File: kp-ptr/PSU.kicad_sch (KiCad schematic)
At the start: 23 parts, among them J2 Conn_01x02, J3 Conn_01x02, U8 AZ1117CH-5.0TRG1, U9 LDFM33PVR

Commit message: Update from v0.1 to v1.0
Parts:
- C35, C36: value 10u -> 10uF 6V3; footprint Capacitor_SMD:C_0402_1005Metric -> Capacitor_SMD:C_0603_1608Metric
- C37: value 1uF -> 100n
- C38: value 1uF -> 100n 50V
- F1: footprint Fuse:Fuse_0805_2012Metric -> Fuse:Fuse_1210_3225Metric
- R19: value 100k -> 100k 1%
- R20: value 10k -> 10k 1%
- R23: value 20k -> 22k
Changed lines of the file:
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@@
     (in_bom yes) (on_board yes)
     (property "Reference" "R23" (id 0) (at 239.395 83.185 90))
-    (property "Value" "20k" (id 1) (at 244.475 83.185 90))
+    (property "Value" "22k" (id 1) (at 244.475 83.185 90))
     (property "Footprint" "Resistor_SMD:R_0402_1005Metric" (id 2) (at 240.157 81.915 90)
       (effects (font (size 1.27 1.27)) hide)
@@
       (effects (font (size 1.27 1.27)) (justify left))
     )
-    (property "Footprint" "Fuse:Fuse_0805_2012Metric" (id 2) (at 181.61 102.235 0)
+    (property "Footprint" "Fuse:Fuse_1210_3225Metric" (id 2) (at 181.61 102.235 0)
       (effects (font (size 1.27 1.27)) (justify left) hide)
     )
@@
   (symbol (lib_id "Device:C") (at 179.07 35.56 0) (mirror y) (unit 1)
     (in_bom yes) (on_board yes) (fields_autoplaced)
-    (property "Reference" "C36" (id 0) (at 175.26 34.2899 0)
-      (effects (font (size 1.27 1.27)) (justify left))
-    )
-    (property "Value" "10u" (id 1) (at 175.26 36.8299 0)
-      (effects (font (size 1.27 1.27)) (justify left))
-    )
-    (property "Footprint" "Capacitor_SMD:C_0402_1005Metric" (id 2) (at 178.1048 39.37 0)
+    (property "Reference" "C36" (id 0) (at 182.88 34.2899 0)
+      (effects (font (size 1.27 1.27)) (justify right))
+    )
+    (property "Value" "10uF 6V3" (id 1) (at 182.88 36.8299 0)
+      (effects (font (size 1.27 1.27)) (justify right))
+    )
+    (property "Footprint" "Capacitor_SMD:C_0603_1608Metric" (id 2) (at 178.1048 39.37 0)
       (effects (font (size 1.27 1.27)) hide)
     )
@@
     (in_bom yes) (on_board yes)
     (property "Reference" "R20" (id 0) (at 29.845 102.87 90))
-    (property "Value" "10k" (id 1) (at 34.925 102.87 90))
+    (property "Value" "10k 1%" (id 1) (at 34.925 102.87 90))
     (property "Footprint" "Resistor_SMD:R_0402_1005Metric" (id 2) (at 30.607 101.6 90)
       (effects (font (size 1.27 1.27)) hide)
@@
   (symbol (lib_id "Device:C") (at 111.76 38.1 0) (mirror y) (unit 1)
     (in_bom yes) (on_board yes) (fields_autoplaced)
-    (property "Reference" "C37" (id 0) (at 107.95 36.8299 0)
-      (effects (font (size 1.27 1.27)) (justify left))
-    )
-    (property "Value" "1uF" (id 1) (at 107.95 39.3699 0)
-      (effects (font (size 1.27 1.27)) (justify left))
+    (property "Reference" "C37" (id 0) (at 115.57 36.8299 0)
+      (effects (font (size 1.27 1.27)) (justify right))
+    )
+    (property "Value" "100n" (id 1) (at 115.57 39.3699 0)
+      (effects (font (size 1.27 1.27)) (justify right))
     )
     (property "Footprint" "Capacitor_SMD:C_0402_1005Metric" (id 2) (at 110.7948 41.91 0)
@@
   (symbol (lib_id "Device:C") (at 182.88 104.775 0) (mirror y) (unit 1)
     (in_bom yes) (on_board yes) (fields_autoplaced)
-    (property "Reference" "C35" (id 0) (at 179.07 103.5049 0)
-      (effects (font (size 1.27 1.27)) (justify left))
-    )
-    (property "Value" "10u" (id 1) (at 179.07 106.0449 0)
-      (effects (font (size 1.27 1.27)) (justify left))
-    )
-    (property "Footprint" "Capacitor_SMD:C_0402_1005Metric" (id 2) (at 181.9148 108.585 0)
+    (property "Reference" "C35" (id 0) (at 186.69 103.5049 0)
+      (effects (font (size 1.27 1.27)) (justify right))
+    )
+    (property "Value" "10uF 6V3" (id 1) (at 186.69 106.0449 0)
+      (effects (font (size 1.27 1.27)) (justify right))
+    )
+    (property "Footprint" "Capacitor_SMD:C_0603_1608Metric" (id 2) (at 181.9148 108.585 0)
       (effects (font (size 1.27 1.27)) hide)
     )
@@
   (symbol (lib_id "Device:C") (at 102.87 104.775 0) (mirror y) (unit 1)
     (in_bom yes) (on_board yes) (fields_autoplaced)
-    (property "Reference" "C38" (id 0) (at 99.06 103.5049 0)
-      (effects (font (size 1.27 1.27)) (justify left))
-    )
-    (property "Value" "1uF" (id 1) (at 99.06 106.0449 0)
-      (effects (font (size 1.27 1.27)) (justify left))
+    (property "Reference" "C38" (id 0) (at 106.68 103.5049 0)
+      (effects (font (size 1.27 1.27)) (justify right))
+    )
+    (property "Value" "100n 50V" (id 1) (at 106.68 106.0449 0)
+      (effects (font (size 1.27 1.27)) (justify right))
     )
     (property "Footprint" "Capacitor_SMD:C_0402_1005Metric" (id 2) (at 101.9048 108.585 0)
@@
     (in_bom yes) (on_board yes)
     (property "Reference" "R19" (id 0) (at 29.845 95.25 90))
-    (property "Value" "100k" (id 1) (at 34.925 95.25 90))
+    (property "Value" "100k 1%" (id 1) (at 34.925 92.71 90))
     (property "Footprint" "Resistor_SMD:R_0402_1005Metric" (id 2) (at 30.607 93.98 90)
       (effects (font (size 1.27 1.27)) hide)

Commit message: Work in progress
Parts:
- F1: footprint Fuse:Fuse_1210_3225Metric -> Fuse:Fuse_1206_3216Metric
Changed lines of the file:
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@@
       (effects (font (size 1.27 1.27)) (justify left))
     )
-    (property "Footprint" "Fuse:Fuse_1210_3225Metric" (id 2) (at 181.61 102.235 0)
+    (property "Footprint" "Fuse:Fuse_1206_3216Metric" (id 2) (at 181.61 102.235 0)
       (effects (font (size 1.27 1.27)) (justify left) hide)
     )

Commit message: Igniters rework v2
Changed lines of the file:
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@@
   (symbol (lib_id "power:+3.3V") (at 252.095 70.485 0) (unit 1)
     (in_bom yes) (on_board yes)
-    (property "Reference" "#PWR099" (id 0) (at 252.095 74.295 0)
+    (property "Reference" "#PWR0101" (id 0) (at 252.095 74.295 0)
       (effects (font (size 1.27 1.27)) hide)
     )
@@
   (symbol (lib_id "power:Earth") (at 182.88 108.585 0) (mirror y) (unit 1)
     (in_bom yes) (on_board yes) (fields_autoplaced)
-    (property "Reference" "#PWR087" (id 0) (at 182.88 114.935 0)
+    (property "Reference" "#PWR0113" (id 0) (at 182.88 114.935 0)
       (effects (font (size 1.27 1.27)) hide)
     )
@@
   (symbol (lib_id "power:VBUS") (at 56.515 33.655 0) (unit 1)
     (in_bom yes) (on_board yes) (fields_autoplaced)
-    (property "Reference" "#PWR082" (id 0) (at 56.515 37.465 0)
+    (property "Reference" "#PWR090" (id 0) (at 56.515 37.465 0)
       (effects (font (size 1.27 1.27)) hide)
     )
@@
   (symbol (lib_id "power:VCC") (at 57.15 44.45 0) (unit 1)
     (in_bom yes) (on_board yes)
-    (property "Reference" "#PWR083" (id 0) (at 57.15 48.26 0)
+    (property "Reference" "#PWR096" (id 0) (at 57.15 48.26 0)
       (effects (font (size 1.27 1.27)) hide)
     )
@@
   (symbol (lib_id "power:Earth") (at 262.255 85.725 0) (unit 1)
     (in_bom yes) (on_board yes) (fields_autoplaced)
-    (property "Reference" "#PWR0102" (id 0) (at 262.255 92.075 0)
+    (property "Reference" "#PWR0105" (id 0) (at 262.255 92.075 0)
       (effects (font (size 1.27 1.27)) hide)
     )
@@
   (symbol (lib_id "power:+3.3V") (at 179.07 31.75 0) (mirror y) (unit 1)
     (in_bom yes) (on_board yes)
-    (property "Reference" "#PWR088" (id 0) (at 179.07 35.56 0)
+    (property "Reference" "#PWR089" (id 0) (at 179.07 35.56 0)
       (effects (font (size 1.27 1.27)) hide)
     )
@@
   (symbol (lib_id "power:VCC") (at 32.385 90.17 0) (unit 1)
     (in_bom yes) (on_board yes)
-    (property "Reference" "#PWR079" (id 0) (at 32.385 93.98 0)
+    (property "Reference" "#PWR0106" (id 0) (at 32.385 93.98 0)
       (effects (font (size 1.27 1.27)) hide)
     )
@@
   (symbol (lib_id "power:+5V") (at 262.255 70.485 0) (unit 1)
     (in_bom yes) (on_board yes)
-    (property "Reference" "#PWR0101" (id 0) (at 262.255 74.295 0)
+    (property "Reference" "#PWR0102" (id 0) (at 262.255 74.295 0)
       (effects (font (size 1.27 1.27)) hide)
     )
@@
   (symbol (lib_id "power:Earth") (at 241.935 85.725 0) (unit 1)
     (in_bom yes) (on_board yes) (fields_autoplaced)
-    (property "Reference" "#PWR098" (id 0) (at 241.935 92.075 0)
+    (property "Reference" "#PWR0103" (id 0) (at 241.935 92.075 0)
       (effects (font (size 1.27 1.27)) hide)
     )
@@
   (symbol (lib_id "power:Earth") (at 102.87 108.585 0) (mirror y) (unit 1)
     (in_bom yes) (on_board yes) (fields_autoplaced)
-    (property "Reference" "#PWR096" (id 0) (at 102.87 114.935 0)
+    (property "Reference" "#PWR0112" (id 0) (at 102.87 114.935 0)
       (effects (font (size 1.27 1.27)) hide)
     )
@@
   (symbol (lib_id "KP-PTR_lib:AZ1117CH-5.0TRG1") (at 165.1 98.425 0) (mirror y) (unit 1)
     (in_bom yes) (on_board yes) (fields_autoplaced)
-    (property "Reference" "U8" (id 0) (at 139.7 86.995 0)
+    (property "Reference" "U8" (id 0) (at 139.7 87.63 0)
       (effects (font (size 1.524 1.524)))
     )
-    (property "Value" "AZ1117CH-5.0TRG1" (id 1) (at 139.7 90.805 0)
+    (property "Value" "AZ1117CH-5.0TRG1" (id 1) (at 139.7 91.44 0)
       (effects (font (size 1.524 1.524)))
     )
@@
   (symbol (lib_id "power:+BATT") (at 31.75 44.45 0) (unit 1)
     (in_bom yes) (on_board yes)
-    (property "Reference" "#PWR077" (id 0) (at 31.75 48.26 0)
+    (property "Reference" "#PWR095" (id 0) (at 31.75 48.26 0)
       (effects (font (size 1.27 1.27)) hide)
     )
@@
   (symbol (lib_id "power:Earth") (at 252.095 85.725 0) (unit 1)
     (in_bom yes) (on_board yes) (fields_autoplaced)
-    (property "Reference" "#PWR0100" (id 0) (at 252.095 92.075 0)
+    (property "Reference" "#PWR0104" (id 0) (at 252.095 92.075 0)
       (effects (font (size 1.27 1.27)) hide)
     )
@@
   (symbol (lib_id "power:+5V") (at 182.88 93.345 0) (mirror y) (unit 1)
     (in_bom yes) (on_board yes) (fields_autoplaced)
-    (property "Reference" "#PWR086" (id 0) (at 182.88 97.155 0)
+    (property "Reference" "#PWR0107" (id 0) (at 182.88 97.155 0)
       (effects (font (size 1.27 1.27)) hide)
     )
@@
   (symbol (lib_id "power:Earth") (at 179.07 39.37 0) (mirror y) (unit 1)
     (in_bom yes) (on_board yes) (fields_autoplaced)
-    (property "Reference" "#PWR089" (id 0) (at 179.07 45.72 0)
+    (property "Reference" "#PWR093" (id 0) (at 179.07 45.72 0)
       (effects (font (size 1.27 1.27)) hide)
     )
@@
   (symbol (lib_id "power:VDD") (at 80.645 44.45 0) (unit 1)
     (in_bom yes) (on_board yes)
-    (property "Reference" "#PWR084" (id 0) (at 80.645 48.26 0)
+    (property "Reference" "#PWR097" (id 0) (at 80.645 48.26 0)
       (effects (font (size 1.27 1.27)) hide)
     )
@@
   (symbol (lib_id "power:Earth") (at 41.275 105.41 0) (unit 1)
     (in_bom yes) (on_board yes) (fields_autoplaced)
-    (property "Reference" "#PWR081" (id 0) (at 41.275 111.76 0)
+    (property "Reference" "#PWR0111" (id 0) (at 41.275 111.76 0)
       (effects (font (size 1.27 1.27)) hide)
     )
@@
   (symbol (lib_id "power:Earth") (at 124.46 31.75 0) (mirror y) (unit 1)
     (in_bom yes) (on_board yes) (fields_autoplaced)
-    (property "Reference" "#PWR091" (id 0) (at 124.46 38.1 0)
+    (property "Reference" "#PWR088" (id 0) (at 124.46 38.1 0)
       (effects (font (size 1.27 1.27)) hide)
     )
@@
   (symbol (lib_id "Device:C_Polarized") (at 80.645 48.26 0) (unit 1)
     (in_bom yes) (on_board yes) (fields_autoplaced)
-    (property "Reference" "C34" (id 0) (at 84.455 46.1009 0)
+    (property "Reference" "C34" (id 0) (at 83.82 46.1009 0)
       (effects (font (size 1.27 1.27)) (justify left))
     )
-    (property "Value" "TBD" (id 1) (at 84.455 48.6409 0)
+    (property "Value" "TBD" (id 1) (at 83.82 48.6409 0)
       (effects (font (size 1.27 1.27)) (justify left))
     )
@@
   (symbol (lib_id "power:VDD") (at 111.76 34.29 0) (mirror y) (unit 1)
     (in_bom yes) (on_board yes)
-    (property "Reference" "#PWR093" (id 0) (at 111.76 38.1 0)
+    (property "Reference" "#PWR091" (id 0) (at 111.76 38.1 0)
       (effects (font (size 1.27 1.27)) hide)
     )
@@
   (symbol (lib_id "power:Earth") (at 80.645 52.07 0) (unit 1)
     (in_bom yes) (on_board yes) (fields_autoplaced)
-    (property "Reference" "#PWR085" (id 0) (at 80.645 58.42 0)
+    (property "Reference" "#PWR099" (id 0) (at 80.645 58.42 0)
       (effects (font (size 1.27 1.27)) hide)
     )
@@
   (symbol (lib_id "power:Earth") (at 31.75 46.99 0) (unit 1)
     (in_bom yes) (on_board yes) (fields_autoplaced)
-    (property "Reference" "#PWR078" (id 0) (at 31.75 53.34 0)
+    (property "Reference" "#PWR098" (id 0) (at 31.75 53.34 0)
       (effects (font (size 1.27 1.27)) hide)
     )
@@
   (symbol (lib_id "power:VDD") (at 241.935 70.485 0) (unit 1)
     (in_bom yes) (on_board yes)
-    (property "Reference" "#PWR097" (id 0) (at 241.935 74.295 0)
+    (property "Reference" "#PWR0100" (id 0) (at 241.935 74.295 0)
       (effects (font (size 1.27 1.27)) hide)
     )
@@
   (symbol (lib_id "power:Earth") (at 32.385 105.41 0) (unit 1)
     (in_bom yes) (on_board yes) (fields_autoplaced)
-    (property "Reference" "#PWR080" (id 0) (at 32.385 111.76 0)
+    (property "Reference" "#PWR0110" (id 0) (at 32.385 111.76 0)
       (effects (font (size 1.27 1.27)) hide)
     )
@@
   (symbol (lib_id "power:VCC") (at 102.87 100.965 0) (unit 1)
     (in_bom yes) (on_board yes)
-    (property "Reference" "#PWR0177" (id 0) (at 102.87 104.775 0)
+    (property "Reference" "#PWR0109" (id 0) (at 102.87 104.775 0)
       (effects (font (size 1.27 1.27)) hide)
     )
@@
   (symbol (lib_id "power:Earth") (at 168.91 98.425 90) (mirror x) (unit 1)
     (in_bom yes) (on_board yes) (fields_autoplaced)
-    (property "Reference" "#PWR090" (id 0) (at 175.26 98.425 0)
-      (effects (font (size 1.27 1.27)) hide)
-    )
+    (property "Reference" "#PWR0108" (id 0) (at 175.26 98.425 0)
+      (effects (font (size 1.27 1.27)) hide)
+    )

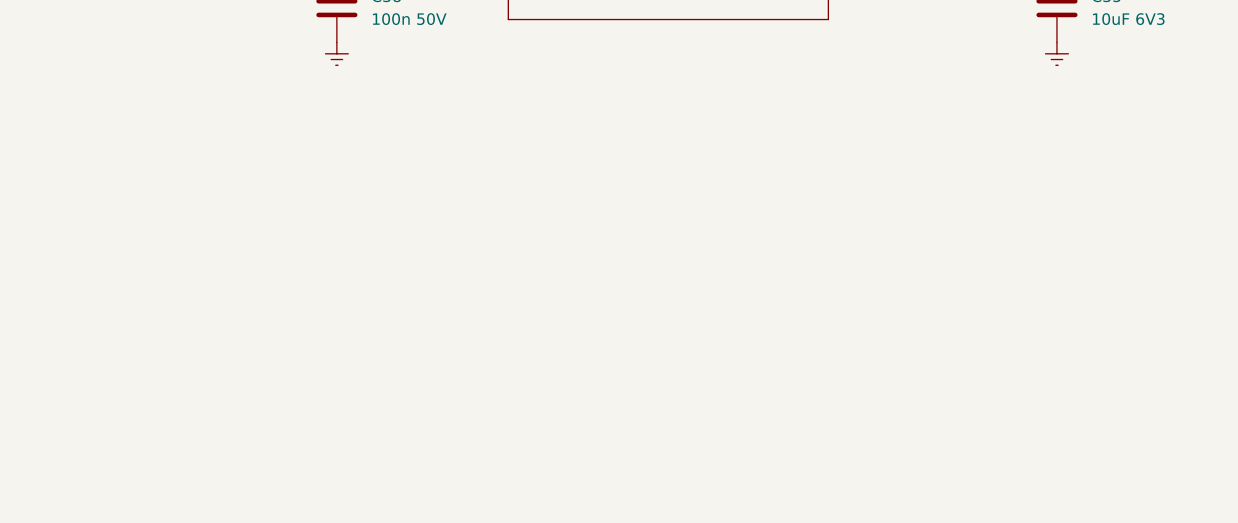
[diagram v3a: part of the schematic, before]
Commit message: DC-DC added
multiple PCB changes
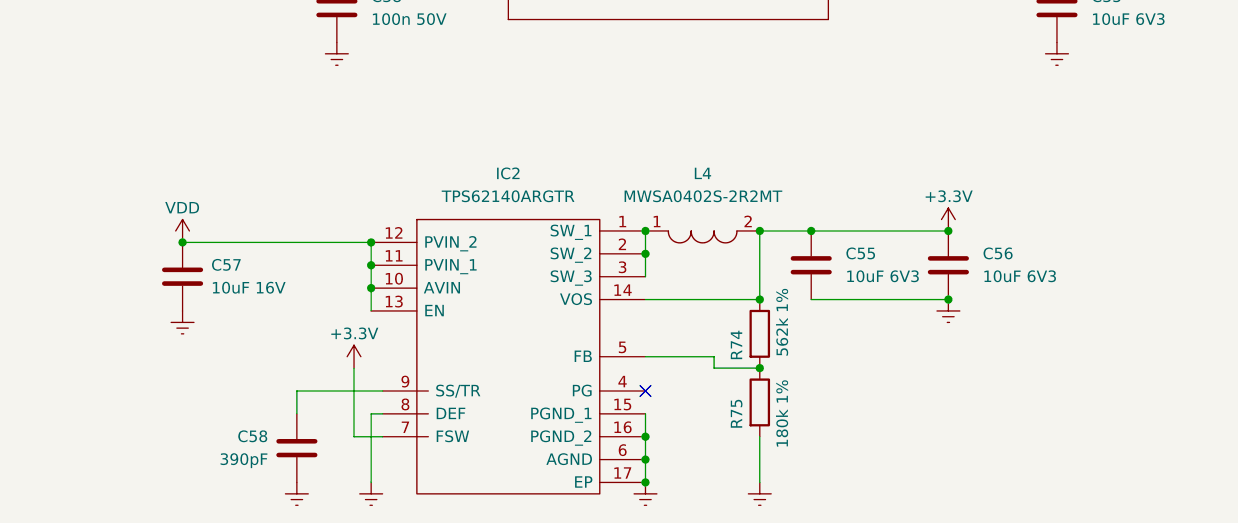
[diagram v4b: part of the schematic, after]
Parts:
- added C55, C56: 10uF 6V3, Capacitor_SMD:C_0603_1608Metric, symbol Device:C
- added C57: 10uF 16V, Capacitor_SMD:C_0603_1608Metric, symbol Device:C
- added C58: 390pF, Capacitor_SMD:C_0402_1005Metric, symbol Device:C
- added IC2: TPS62140ARGTR, KP-PTR_lib:QFN50P300X300X100-17N-D, symbol KP-PTR_lib:TPS62140ARGTR
- added L4: MWSA0402S-2R2MT, KP-PTR_lib:INDPM4442X200N, symbol KP-PTR_lib:MWSA0402S-2R2MT
- added R74: 562k 1%, Resistor_SMD:R_0402_1005Metric, symbol Device:R
- added R75: 180k 1%, Resistor_SMD:R_0402_1005Metric, symbol Device:R
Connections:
- net +3V3: now also C55.1, C56.1, IC2.14 (VOS), IC2.7 (FSW), L4.2, R74.1
- net Earth: now also C55.2, C56.2, C57.2, C58.1, IC2.15 (PGND_1), IC2.16 (PGND_2), IC2.17 (EP), IC2.6 (AGND), IC2.8 (DEF), R75.2
- net VDD: now also C57.1, IC2.10 (AVIN), IC2.11 (PVIN_1), IC2.12 (PVIN_2), IC2.13 (EN)
- new net: C58.2, IC2.9 (SS/TR)
- new net: IC2.5 (FB), R74.2, R75.1
- new net: IC2.1 (SW_1), IC2.2 (SW_2), IC2.3 (SW_3), L4.1
- no-connect marks 2 -> 3

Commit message: Parts renumbered! Noice!
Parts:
- renumbered C34 to C38, C33 to C39, C38 to C40, C35 to C41, C55 to C42, C56 to C43, C57 to C44, C58 to C45, IC2 to IC1, R21 to R27, R23 to R28, R24 to R29, R25 to R30, R19 to R31, R22 to R32, R20 to R33, R74 to R34, R75 to R35, U8 to U10

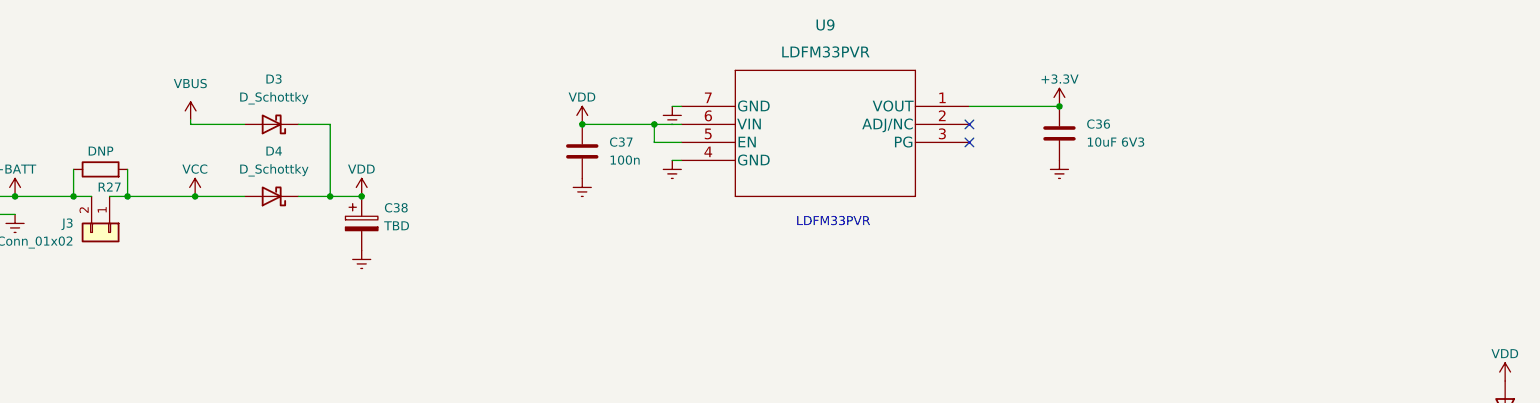
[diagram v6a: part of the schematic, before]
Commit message: Backup capacitor changed from electro to tantal.
Multiple kung fu changes
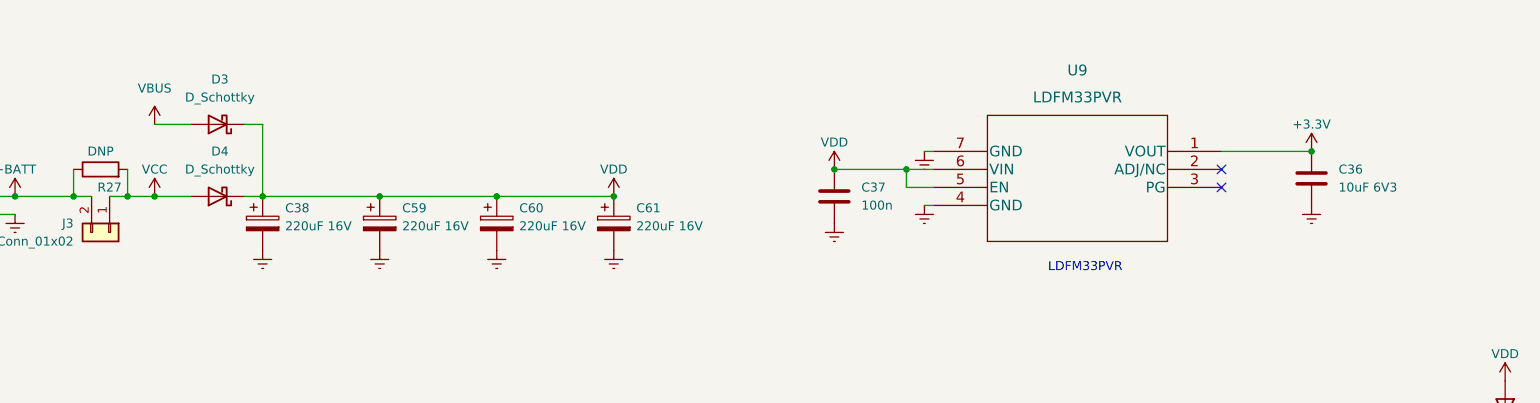
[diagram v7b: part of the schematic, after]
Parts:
- added C59, C60, C61: 220uF 16V, Capacitor_Tantalum_SMD:CP_EIA-7343-31_Kemet-D, symbol Device:C_Polarized
- C38: value TBD -> 220uF 16V; footprint Capacitor_SMD:CP_Elec_10x10 -> Capacitor_Tantalum_SMD:CP_EIA-7343-31_Kemet-D
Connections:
- net Earth: now also C59.2, C60.2, C61.2
- net VDD: now also C59.1, C60.1, C61.1
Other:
- moved on the sheet: C36, C37, C38, D3, D4, U9
